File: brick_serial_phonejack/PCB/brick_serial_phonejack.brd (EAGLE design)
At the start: 27.9 x 39.4 mm, 11 parts, among them J1 0

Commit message: Change resistance value
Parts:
- R3: value 5.1k -> 4.7k
- R4: value 3.3k -> 3k
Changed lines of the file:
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@@
 <element name="R1" library="gclue" package="EIA0603-RES" value="100k" x="23" y="18.5"/>
 <element name="R2" library="gclue" package="EIA0603-RES" value="22k" x="17.5" y="23.5"/>
-<element name="R3" library="gclue" package="EIA0603-RES" value="5.1k" x="6.5" y="23.5"/>
-<element name="R4" library="gclue" package="EIA0603-RES" value="3.3k" x="11.5" y="23.5"/>
+<element name="R3" library="gclue" package="EIA0603-RES" value="4.7k" x="6.5" y="23.5"/>
+<element name="R4" library="gclue" package="EIA0603-RES" value="3k" x="11.5" y="23.5"/>
 <element name="C2" library="gclue" package="EIA0603-CAP" value="1u" x="6.5" y="18.5"/>
 <element name="J1" library="gclue" package="BRICK_SERIAL" value="0" x="14.5" y="22.5"/>

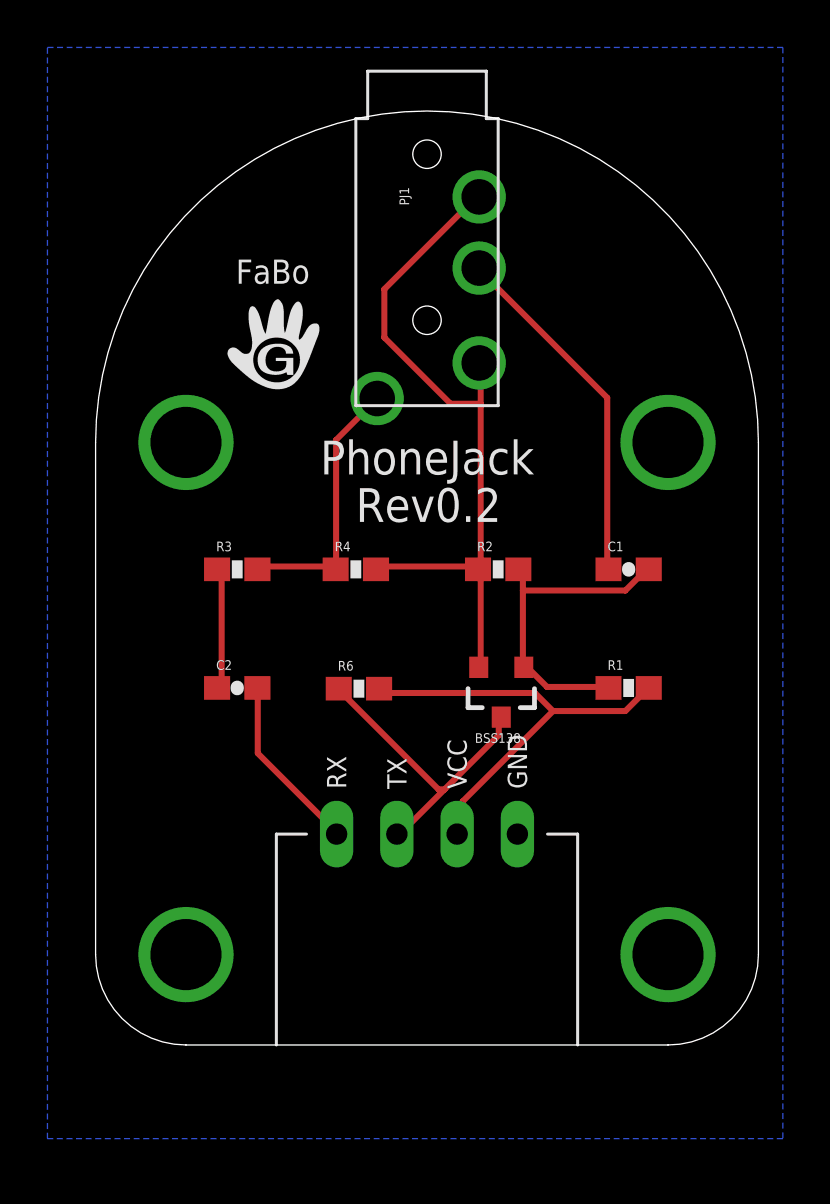
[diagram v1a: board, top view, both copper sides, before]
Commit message: refine board brick_serial_phonejack
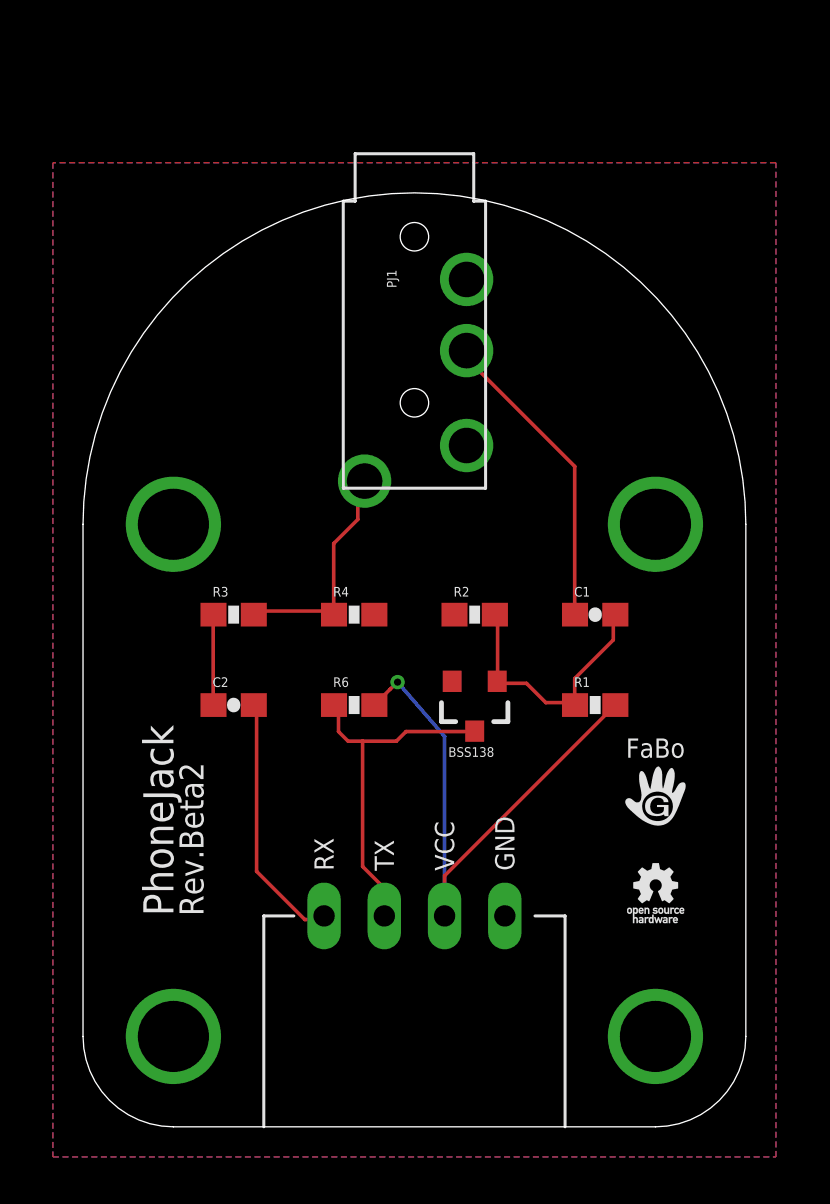
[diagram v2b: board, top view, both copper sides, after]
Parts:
- removed U$1: (no value), gclue:LOGO_FABO_M
- added U$2: (no value), gclue:LOGO_OSHW_T_S
- added U$5: A4L-LOC-FABO_S, gclue:LOGO_FABO_S
- moved PJ1 3.52 mm to (14.0, 33.0)
- moved J1 3.49 mm to (14.0, 19.1)
- moved C1 2.37 mm to (21.6, 21.6)
- moved R2 2.15 mm to (16.5, 21.6)
- moved R3 1.92 mm to (6.35, 21.6)
- moved R4 1.91 mm to (11.4, 21.6)
- moved R1 1.58 mm to (21.6, 17.8)
- moved BSS138 1.27 mm to (16.5, 17.8)
- moved C2 0.74 mm to (6.35, 17.8)
- moved R6 0.72 mm to (11.4, 17.8)
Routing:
- net GND: track 30.0 -> 0.00 mm
- net +5V: track 19.1 -> 23.8 mm, vias 0 -> 1
- net RX: track 7.53 -> 10.9 mm
- net TX_LV: track 13.8 -> 11.1 mm
- net TX_HV: track 13.0 -> 15.1 mm
- net N$2: track 14.9 -> 13.1 mm
- net MIC: track 11.4 -> 9.60 mm
- net N$1: track 5.26 -> 3.81 mm
- added copper zone on layer 1, net GND
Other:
- board text added: "Rev.Beta2"
- board text removed: "Rev0.2"

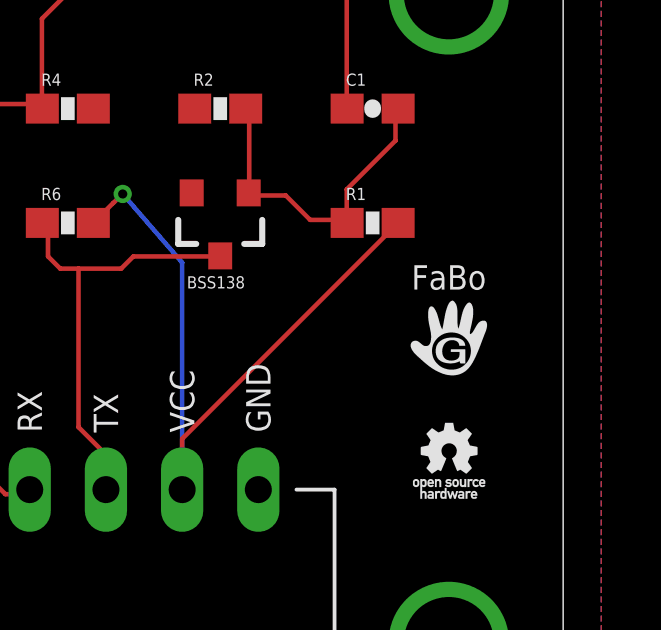
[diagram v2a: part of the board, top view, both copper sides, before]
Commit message: change logo
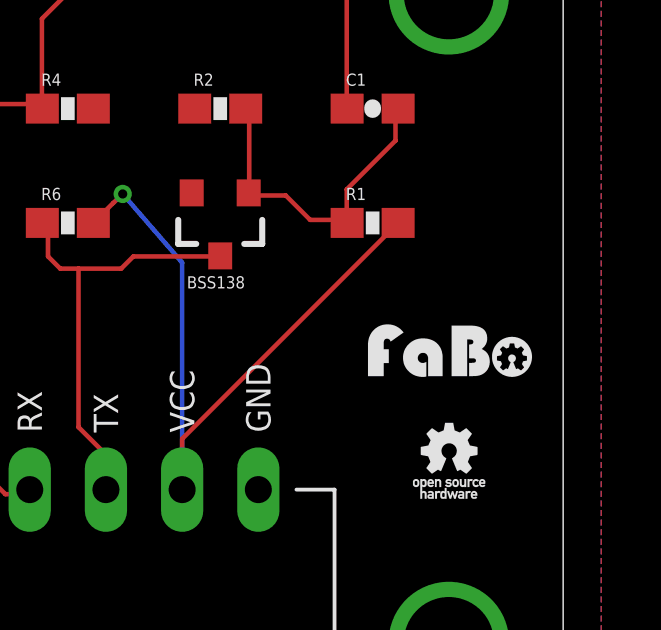
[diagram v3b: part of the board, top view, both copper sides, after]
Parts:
- removed U$5: A4L-LOC-FABO_S, gclue:LOGO_FABO_S
- added U$1: (no value), FaBo:LOGO_FABO_S
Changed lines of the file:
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@@
 <setting verticaltext="up"/>
 </settings>
-<grid distance="6" unitdist="mil" unit="mil" style="lines" multiple="1" display="yes" altdistance="0.025" altunitdist="inch" altunit="inch"/>
+<grid distance="0.05" unitdist="inch" unit="inch" style="lines" multiple="1" display="yes" altdistance="0.025" altunitdist="inch" altunit="inch"/>
 <layers>
 <layer number="1" name="Top" color="4" fill="1" visible="yes" active="yes"/>
@@
 <element name="C2" library="gclue" package="EIA0603-CAP" value="1u" x="6.35" y="17.78"/>
 <element name="J1" library="gclue" package="BRICK_SERIAL" value="0" x="13.97" y="19.05"/>
-<element name="U$5" library="gclue" package="LOGO_FABO_S" value="A4L-LOC-FABO_S" x="24.13" y="13.97"/>
 <element name="U$2" library="gclue" package="LOGO_OSHW_T_S" value="" x="24.13" y="10.16"/>
+<element name="U$1" library="FaBo" package="LOGO_FABO_S" value="" x="24.2316" y="12.6492"/>
 </elements>
 <signals>

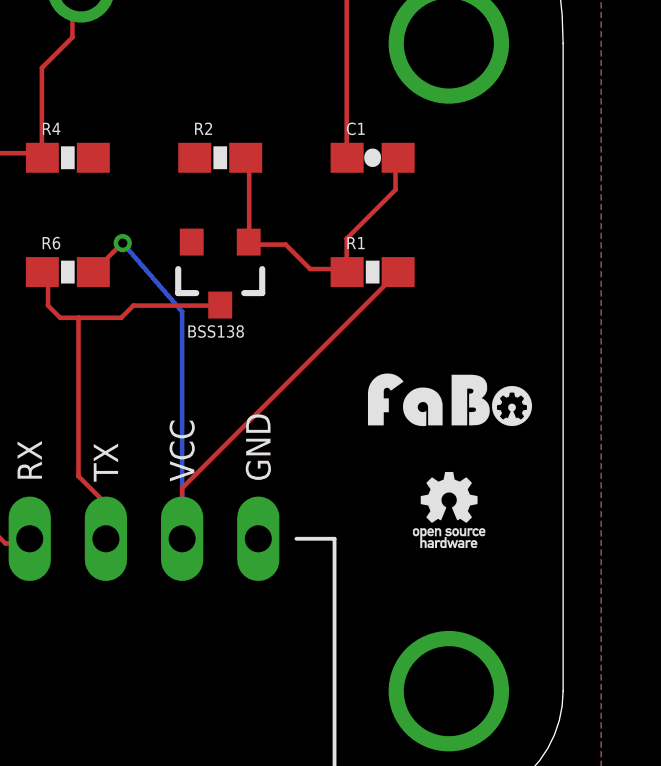
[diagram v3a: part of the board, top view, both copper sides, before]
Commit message: add made-in-japan logo
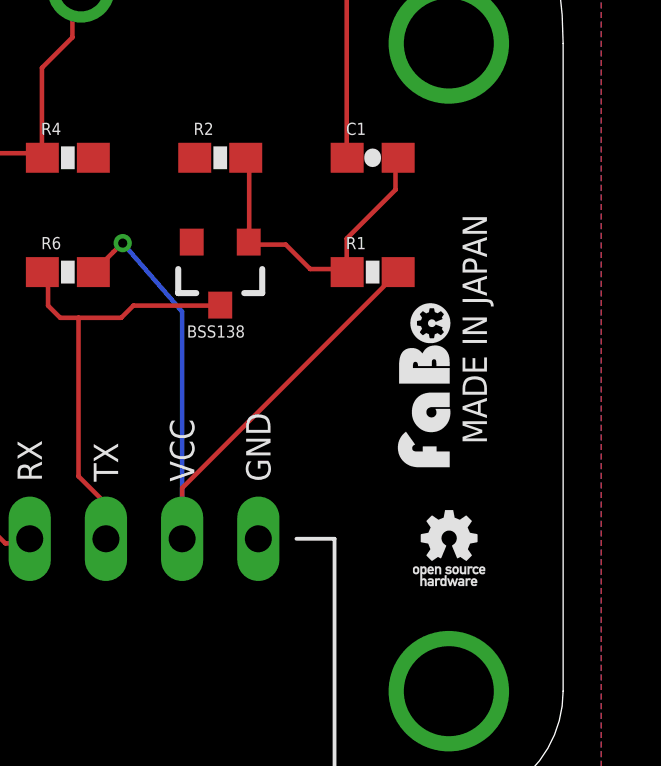
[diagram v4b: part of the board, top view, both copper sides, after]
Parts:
- moved U$1 1.42 mm to (24.2, 14.1), turned to 90 degrees
- moved U$2 1.27 mm to (24.1, 8.89)
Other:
- board text added: "MADE IN JAPAN"
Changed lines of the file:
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@@
 <text x="5.08" y="8.89" size="1.016" layer="21" font="vector" rot="R90">Rev.Beta2</text>
 <text x="3.81" y="8.89" size="1.27" layer="21" font="vector" rot="R90">PhoneJack</text>
+<text x="25.4" y="15.875" size="0.8128" layer="21" font="vector" rot="R90" align="bottom-center">MADE IN JAPAN</text>
 </plain>
 <attributes>
@@
 <element name="C2" library="gclue" package="EIA0603-CAP" value="1u" x="6.35" y="17.78"/>
 <element name="J1" library="gclue" package="BRICK_SERIAL" value="0" x="13.97" y="19.05"/>
-<element name="U$2" library="gclue" package="LOGO_OSHW_T_S" value="" x="24.13" y="10.16"/>
-<element name="U$1" library="FaBo" package="LOGO_FABO_S" value="" x="24.2316" y="12.6492"/>
+<element name="U$2" library="gclue" package="LOGO_OSHW_T_S" value="" x="24.13" y="8.89"/>
+<element name="U$1" library="FaBo" package="LOGO_FABO_S" value="" x="24.1808" y="14.0716" rot="R90"/>
 </elements>
 <signals>
